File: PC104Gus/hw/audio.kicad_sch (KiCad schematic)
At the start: 12 parts, among them U9 PCM5100

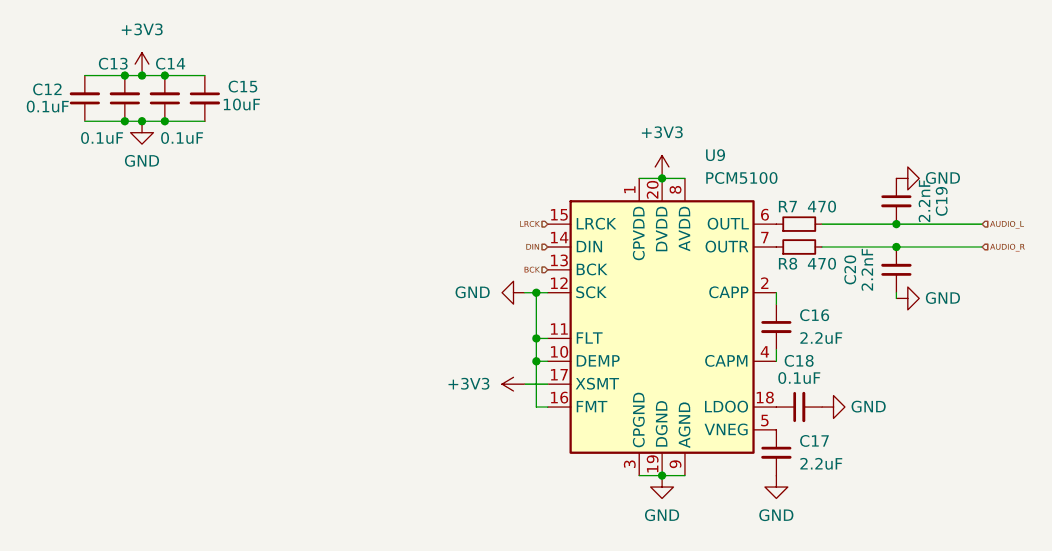
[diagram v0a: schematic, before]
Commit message: Part position complete
Added all parts, sorted part numbering and foot prints.
Beginning routing
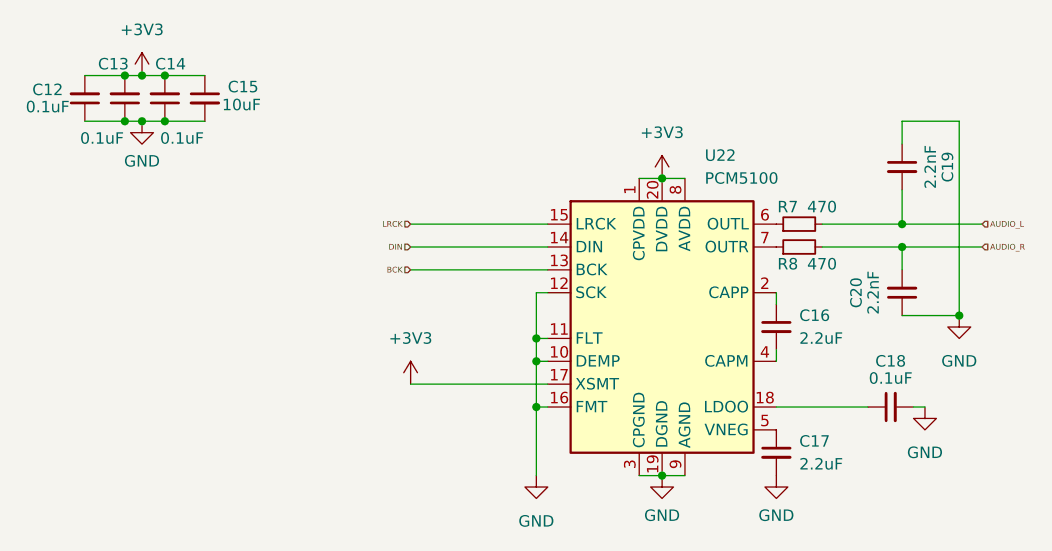
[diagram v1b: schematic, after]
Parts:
- renumbered U9 to U22
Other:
- moved on the sheet: C18, C19, C20

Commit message: PC104GUS production files
Production files generated. This build worked!
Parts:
- C12, C13, C14, C18: LCSC (none) -> C49678
- C15: LCSC (none) -> C15850
- C16, C17: LCSC (none) -> C377773
- C19, C20: LCSC (none) -> C28260
- R7, R8: LCSC (none) -> C17710
- U22: LCSC (none) -> C131154
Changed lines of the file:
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@@
+			)
+		)
+		(property "LCSC" "C28260"
+			(at 163.83 86.36 90)
+			(effects
+				(font
+					(size 1.27 1.27)
+				)
+				(hide yes)
 			)
 		)
@@
 			)
 		)
+		(property "LCSC" "C49678"
+			(at 73.025 64.77 0)
+			(effects
+				(font
+					(size 1.27 1.27)
+				)
+				(hide yes)
+			)
+		)
 		(pin "1"
 		)
@@
 					(size 1.27 1.27)
 				)
+			)
+		)
+		(property "LCSC" "C49678"
+			(at 162.56 99.06 90)
+			(effects
+				(font
+					(size 1.27 1.27)
+				)
+				(hide yes)
 			)
 		)
@@
 			)
 		)
+		(property "LCSC" "C377773"
+			(at 149.86 90.17 0)
+			(effects
+				(font
+					(size 1.27 1.27)
+				)
+				(hide yes)
+			)
+		)
 		(pin "1"
 		)
@@
 					(size 1.27 1.27)
 				)
+			)
+		)
+		(property "LCSC" "C28260"
+			(at 163.83 72.39 90)
+			(effects
+				(font
+					(size 1.27 1.27)
+				)
+				(hide yes)
 			)
 		)
@@
 			)
 		)
+		(property "LCSC" "C49678"
+			(at 77.47 64.77 0)
+			(effects
+				(font
+					(size 1.27 1.27)
+				)
+				(hide yes)
+			)
+		)
 		(pin "1"
 		)
@@
 					(size 1.27 1.27)
 				)
+			)
+		)
+		(property "LCSC" "C15850"
+			(at 86.36 64.77 0)
+			(effects
+				(font
+					(size 1.27 1.27)
+				)
+				(hide yes)
 			)
 		)
@@
 			)
 		)
+		(property "LCSC" "C377773"
+			(at 149.86 104.14 0)
+			(effects
+				(font
+					(size 1.27 1.27)
+				)
+				(hide yes)
+			)
+		)
 		(pin "1"
 		)
@@
 			)
 		)
+		(property "LCSC" "C131154"
+			(at 137.16 88.9 0)
+			(effects
+				(font
+					(size 1.27 1.27)
+				)
+				(hide yes)
+			)
+		)
 		(pin "1"
 		)
@@
 			)
 		)
+		(property "LCSC" "C17710"
+			(at 152.4 81.28 90)
+			(effects
+				(font
+					(size 1.27 1.27)
+				)
+				(hide yes)
+			)
+		)
 		(pin "1"
 		)
@@
 			)
 		)
+		(property "LCSC" "C49678"
+			(at 81.915 64.77 0)
+			(effects
+				(font
+					(size 1.27 1.27)
+				)
+				(hide yes)
+			)
+		)
 		(pin "1"
 		)
@@
 			)
 		)
+		(property "LCSC" "C17710"
+			(at 152.4 78.74 90)
+			(effects
+				(font
+					(size 1.27 1.27)
+				)
+				(hide yes)
+			)
+		)
